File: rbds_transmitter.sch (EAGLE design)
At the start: 50 parts, among them IC1 MAX1551, IC2 TPS61030, IC3 MCP4812, IC4 OPA4743UA, Q1 P-Ch, SW1 FSMSM, U3 ATMEGA328, X1 HD44780LCD-1602, Y1 16Mhz

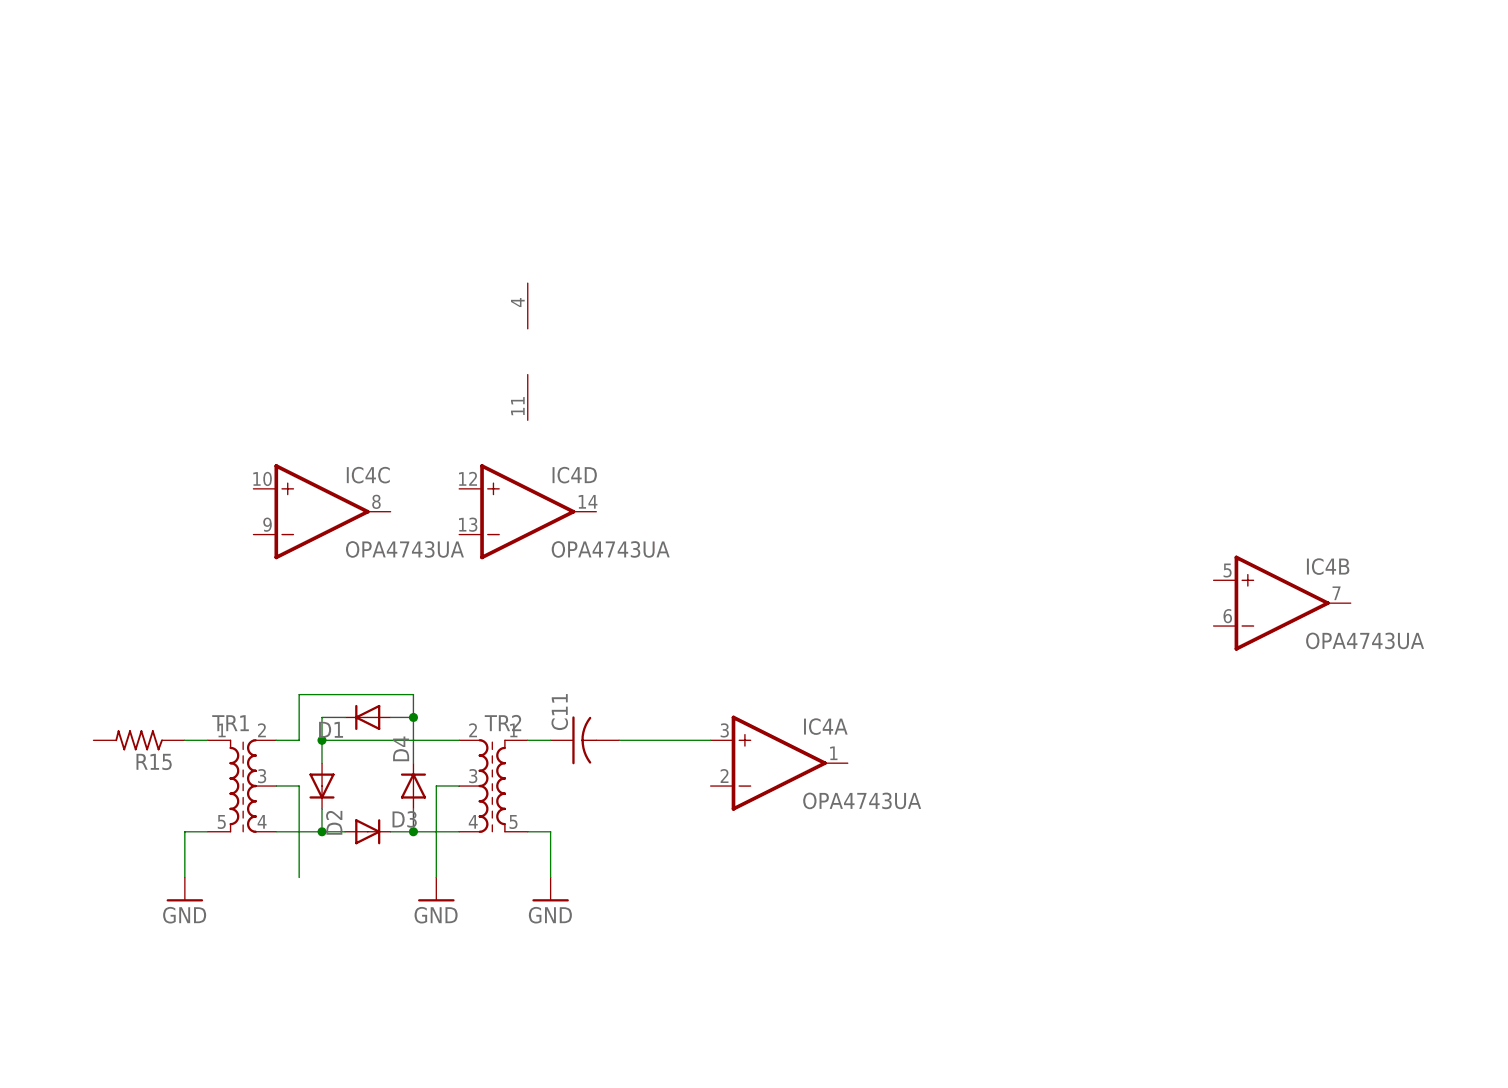
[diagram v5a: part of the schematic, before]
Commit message: adding summing amp
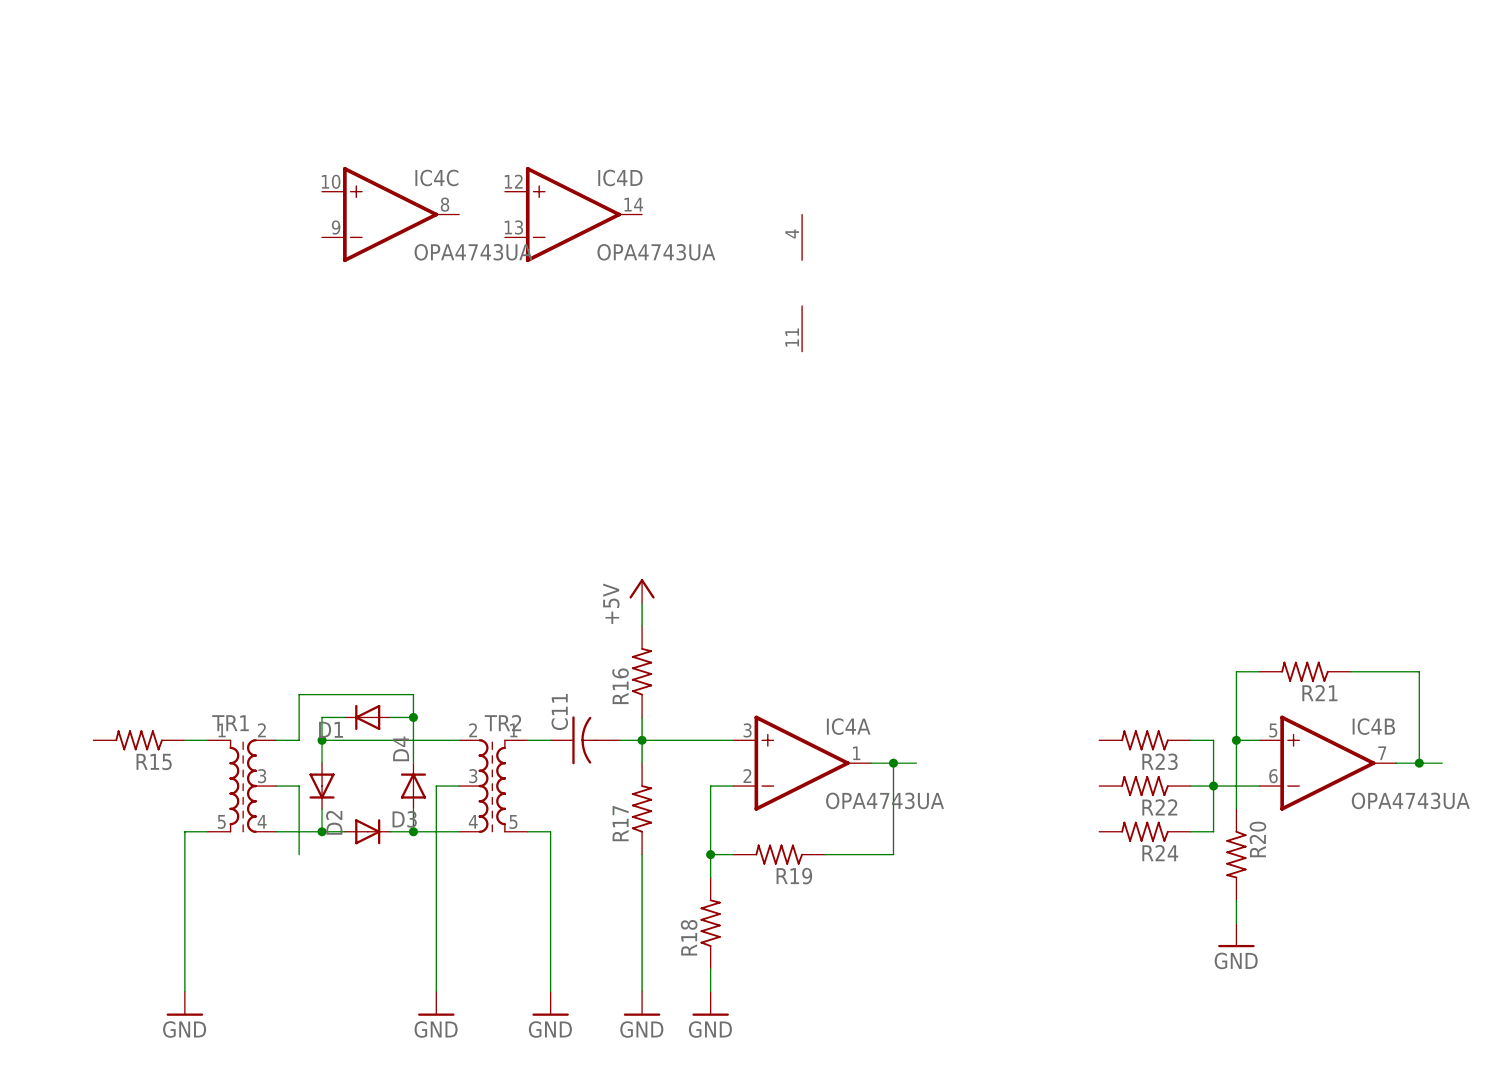
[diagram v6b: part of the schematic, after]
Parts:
- added R16, R17, R18, R19, R20, R21, R22, R23, R24: (no value), adafruit:R-US_R1206
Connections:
- new net N$23: IC4B.+IN, R20.1, R21.2
- new net N$24: IC4A.-IN, R18.2, R19.2
- new net N$25: IC4A.OUT, R19.1
- new net N$26: IC4B.OUT, R21.1
- new net N$27: IC4B.-IN, R22.1, R23.1, R24.1
- net +5V: now also R16.2
- net GND: now also R17.1, R18.1, R20.2
- net N$22: now also R16.1, R17.2
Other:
- moved on the sheet: IC4A, IC4B, IC4C, IC4D
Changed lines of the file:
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@@
 <part name="C11" library="adafruit" deviceset="C-US" device="C1206"/>
 <part name="IC4" library="linear" deviceset="OPA4743" device="UA"/>
+<part name="R16" library="adafruit" deviceset="R-US_" device="R1206"/>
+<part name="R17" library="adafruit" deviceset="R-US_" device="R1206"/>
+<part name="GND26" library="sparkfun" deviceset="GND" device=""/>
+<part name="P+9" library="supply1" deviceset="+5V" device=""/>
+<part name="R18" library="adafruit" deviceset="R-US_" device="R1206"/>
+<part name="R19" library="adafruit" deviceset="R-US_" device="R1206"/>
+<part name="GND27" library="sparkfun" deviceset="GND" device=""/>
+<part name="R20" library="adafruit" deviceset="R-US_" device="R1206"/>
+<part name="R21" library="adafruit" deviceset="R-US_" device="R1206"/>
+<part name="R22" library="adafruit" deviceset="R-US_" device="R1206"/>
+<part name="GND28" library="sparkfun" deviceset="GND" device=""/>
+<part name="R23" library="adafruit" deviceset="R-US_" device="R1206"/>
+<part name="R24" library="adafruit" deviceset="R-US_" device="R1206"/>
 </parts>
 <sheets>
@@
 <instance part="TR1" gate="G$1" x="254" y="-15.24"/>
 <instance part="TR2" gate="G$1" x="279.4" y="-15.24" rot="MR0"/>
-<instance part="GND23" gate="1" x="246.38" y="-27.94"/>
-<instance part="GND24" gate="1" x="274.32" y="-27.94"/>
-<instance part="GND25" gate="1" x="287.02" y="-27.94"/>
+<instance part="GND23" gate="1" x="246.38" y="-40.64"/>
+<instance part="GND24" gate="1" x="274.32" y="-40.64"/>
+<instance part="GND25" gate="1" x="287.02" y="-40.64"/>
 <instance part="R15" gate="G$1" x="241.3" y="-10.16" rot="R180"/>
 <instance part="C11" gate="G$1" x="289.56" y="-10.16" rot="R90"/>
-<instance part="IC4" gate="A" x="312.42" y="-12.7"/>
-<instance part="IC4" gate="B" x="368.3" y="5.08"/>
-<instance part="IC4" gate="C" x="261.62" y="15.24"/>
-<instance part="IC4" gate="D" x="284.48" y="15.24"/>
-<instance part="IC4" gate="P" x="284.48" y="33.02"/>
+<instance part="IC4" gate="A" x="314.96" y="-12.7"/>
+<instance part="IC4" gate="B" x="373.38" y="-12.7"/>
+<instance part="IC4" gate="C" x="269.24" y="48.26"/>
+<instance part="IC4" gate="D" x="289.56" y="48.26"/>
+<instance part="IC4" gate="P" x="314.96" y="40.64"/>
+<instance part="R16" gate="G$1" x="297.18" y="-2.54" rot="R90"/>
+<instance part="R17" gate="G$1" x="297.18" y="-17.78" rot="R90"/>
+<instance part="GND26" gate="1" x="297.18" y="-40.64"/>
+<instance part="P+9" gate="1" x="297.18" y="7.62"/>
+<instance part="R18" gate="G$1" x="304.8" y="-30.48" rot="R90"/>
+<instance part="R19" gate="G$1" x="312.42" y="-22.86" rot="R180"/>
+<instance part="GND27" gate="1" x="304.8" y="-40.64"/>
+<instance part="R20" gate="G$1" x="363.22" y="-22.86" rot="R270"/>
+<instance part="R21" gate="G$1" x="370.84" y="-2.54" rot="R180"/>
+<instance part="R22" gate="G$1" x="353.06" y="-15.24" rot="R180"/>
+<instance part="GND28" gate="1" x="363.22" y="-33.02"/>
+<instance part="R23" gate="G$1" x="353.06" y="-10.16" rot="R180"/>
+<instance part="R24" gate="G$1" x="353.06" y="-20.32" rot="R180"/>
 </instances>
 <busses>
@@
 <pinref part="TR1" gate="G$1" pin="5"/>
 <pinref part="GND23" gate="1" pin="GND"/>
-<wire x1="246.38" y1="-25.4" x2="246.38" y2="-20.32" width="0.1524" layer="91"/>
+<wire x1="246.38" y1="-38.1" x2="246.38" y2="-20.32" width="0.1524" layer="91"/>
 <wire x1="246.38" y1="-20.32" x2="248.92" y2="-20.32" width="0.1524" layer="91"/>
 </segment>
@@
 <pinref part="TR2" gate="G$1" pin="3"/>
 <wire x1="276.86" y1="-15.24" x2="274.32" y2="-15.24" width="0.1524" layer="91"/>
-<wire x1="274.32" y1="-15.24" x2="274.32" y2="-25.4" width="0.1524" layer="91"/>
+<wire x1="274.32" y1="-15.24" x2="274.32" y2="-38.1" width="0.1524" layer="91"/>
 <pinref part="GND24" gate="1" pin="GND"/>
 </segment>
@@
 <pinref part="TR2" gate="G$1" pin="5"/>
 <pinref part="GND25" gate="1" pin="GND"/>
-<wire x1="287.02" y1="-25.4" x2="287.02" y2="-20.32" width="0.1524" layer="91"/>
+<wire x1="287.02" y1="-38.1" x2="287.02" y2="-20.32" width="0.1524" layer="91"/>
 <wire x1="287.02" y1="-20.32" x2="284.48" y2="-20.32" width="0.1524" layer="91"/>
+</segment>
+<segment>
+<pinref part="R17" gate="G$1" pin="1"/>
+<pinref part="GND26" gate="1" pin="GND"/>
+<wire x1="297.18" y1="-38.1" x2="297.18" y2="-22.86" width="0.1524" layer="91"/>
+</segment>
+<segment>
+<pinref part="R18" gate="G$1" pin="1"/>
+<pinref part="GND27" gate="1" pin="GND"/>
+<wire x1="304.8" y1="-38.1" x2="304.8" y2="-35.56" width="0.1524" layer="91"/>
+</segment>
+<segment>
+<pinref part="R20" gate="G$1" pin="2"/>
+<pinref part="GND28" gate="1" pin="GND"/>
+<wire x1="363.22" y1="-30.48" x2="363.22" y2="-27.94" width="0.1524" layer="91"/>
 </segment>
 </net>
@@
 <wire x1="157.48" y1="-2.54" x2="157.48" y2="-5.08" width="0.1524" layer="91"/>
 </segment>
+<segment>
+<pinref part="R16" gate="G$1" pin="2"/>
+<pinref part="P+9" gate="1" pin="+5V"/>
+<wire x1="297.18" y1="5.08" x2="297.18" y2="2.54" width="0.1524" layer="91"/>
+</segment>
 </net>
 <net name="ISP-MISO" class="0">
@@
 <pinref part="TR1" gate="G$1" pin="3"/>
 <wire x1="256.54" y1="-15.24" x2="259.08" y2="-15.24" width="0.1524" layer="91"/>
-<wire x1="259.08" y1="-15.24" x2="259.08" y2="-25.4" width="0.1524" layer="91"/>
+<wire x1="259.08" y1="-15.24" x2="259.08" y2="-22.86" width="0.1524" layer="91"/>
 </segment>
 </net>
@@
 <segment>
 <pinref part="C11" gate="G$1" pin="2"/>
-<wire x1="294.64" y1="-10.16" x2="304.8" y2="-10.16" width="0.1524" layer="91"/>
 <pinref part="IC4" gate="A" pin="+IN"/>
-</segment>
-</net>
+<wire x1="294.64" y1="-10.16" x2="297.18" y2="-10.16" width="0.1524" layer="91"/>
+<pinref part="R16" gate="G$1" pin="1"/>
+<pinref part="R17" gate="G$1" pin="2"/>
+<wire x1="297.18" y1="-10.16" x2="307.34" y2="-10.16" width="0.1524" layer="91"/>
+<wire x1="297.18" y1="-7.62" x2="297.18" y2="-10.16" width="0.1524" layer="91"/>
+<junction x="297.18" y="-10.16"/>
+<wire x1="297.18" y1="-10.16" x2="297.18" y2="-12.7" width="0.1524" layer="91"/>
+</segment>
+</net>
+<net name="N$24" class="0">
+<segment>
+<pinref part="R18" gate="G$1" pin="2"/>
+<wire x1="304.8" y1="-25.4" x2="304.8" y2="-22.86" width="0.1524" layer="91"/>
+<pinref part="IC4" gate="A" pin="-IN"/>
+<wire x1="304.8" y1="-22.86" x2="304.8" y2="-15.24" width="0.1524" layer="91"/>
+<wire x1="304.8" y1="-15.24" x2="307.34" y2="-15.24" width="0.1524" layer="91"/>
+<pinref part="R19" gate="G$1" pin="2"/>
+<wire x1="307.34" y1="-22.86" x2="304.8" y2="-22.86" width="0.1524" layer="91"/>
+<junction x="304.8" y="-22.86"/>
+</segment>
+</net>
+<net name="N$25" class="0">
+<segment>
+<pinref part="R19" gate="G$1" pin="1"/>
+<wire x1="317.5" y1="-22.86" x2="325.12" y2="-22.86" width="0.1524" layer="91"/>
+<wire x1="325.12" y1="-22.86" x2="325.12" y2="-12.7" width="0.1524" layer="91"/>
+<pinref part="IC4" gate="A" pin="OUT"/>
+<wire x1="325.12" y1="-12.7" x2="322.58" y2="-12.7" width="0.1524" layer="91"/>
+<wire x1="325.12" y1="-12.7" x2="327.66" y2="-12.7" width="0.1524" layer="91"/>
+<junction x="325.12" y="-12.7"/>
+</segment>
+</net>
+<net name="N$23" class="0">
+<segment>
+<pinref part="IC4" gate="B" pin="+IN"/>
+<pinref part="R20" gate="G$1" pin="1"/>
+<wire x1="363.22" y1="-17.78" x2="363.22" y2="-10.16" width="0.1524" layer="91"/>
+<wire x1="363.22" y1="-10.16" x2="365.76" y2="-10.16" width="0.1524" layer="91"/>
+<junction x="363.22" y="-10.16"/>
+<wire x1="363.22" y1="-10.16" x2="363.22" y2="-2.54" width="0.1524" layer="91"/>
+<pinref part="R21" gate="G$1" pin="2"/>
+<wire x1="363.22" y1="-2.54" x2="365.76" y2="-2.54" width="0.1524" layer="91"/>
+</segment>
+</net>
+<net name="N$26" class="0">
+<segment>
+<pinref part="R21" gate="G$1" pin="1"/>
+<wire x1="375.92" y1="-2.54" x2="383.54" y2="-2.54" width="0.1524" layer="91"/>
+<wire x1="383.54" y1="-2.54" x2="383.54" y2="-12.7" width="0.1524" layer="91"/>
+<pinref part="IC4" gate="B" pin="OUT"/>
+<wire x1="383.54" y1="-12.7" x2="381" y2="-12.7" width="0.1524" layer="91"/>
+<wire x1="383.54" y1="-12.7" x2="386.08" y2="-12.7" width="0.1524" layer="91"/>
+<junction x="383.54" y="-12.7"/>
+</segment>
+</net>
+<net name="N$27" class="0">
+<segment>
+<pinref part="IC4" gate="B" pin="-IN"/>
+<wire x1="365.76" y1="-15.24" x2="360.68" y2="-15.24" width="0.1524" layer="91"/>
+<pinref part="R22" gate="G$1" pin="1"/>
+<junction x="360.68" y="-15.24"/>
+<wire x1="360.68" y1="-15.24" x2="358.14" y2="-15.24" width="0.1524" layer="91"/>
+<pinref part="R24" gate="G$1" pin="1"/>
+<wire x1="358.14" y1="-20.32" x2="360.68" y2="-20.32" width="0.1524" layer="91"/>
+<wire x1="360.68" y1="-20.32" x2="360.68" y2="-15.24" width="0.1524" layer="91"/>
+<pinref part="R23" gate="G$1" pin="1"/>
+<wire x1="358.14" y1="-10.16" x2="360.68" y2="-10.16" width="0.1524" layer="91"/>
+<wire x1="360.68" y1="-10.16" x2="360.68" y2="-15.24" width="0.1524" layer="91"/>
+</segment>
+</net>

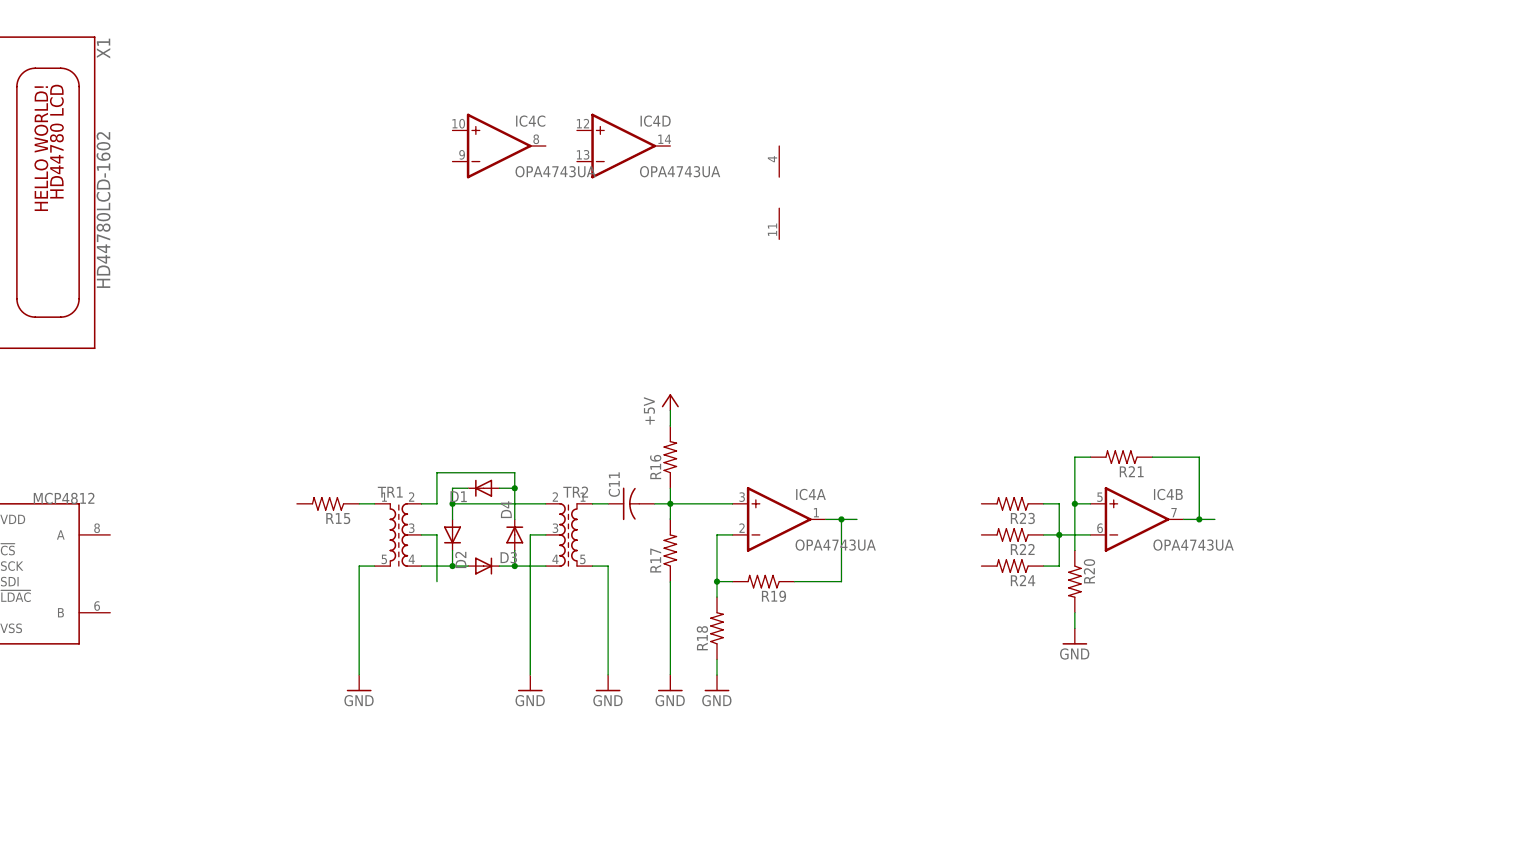
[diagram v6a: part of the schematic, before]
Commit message: added low pass filter
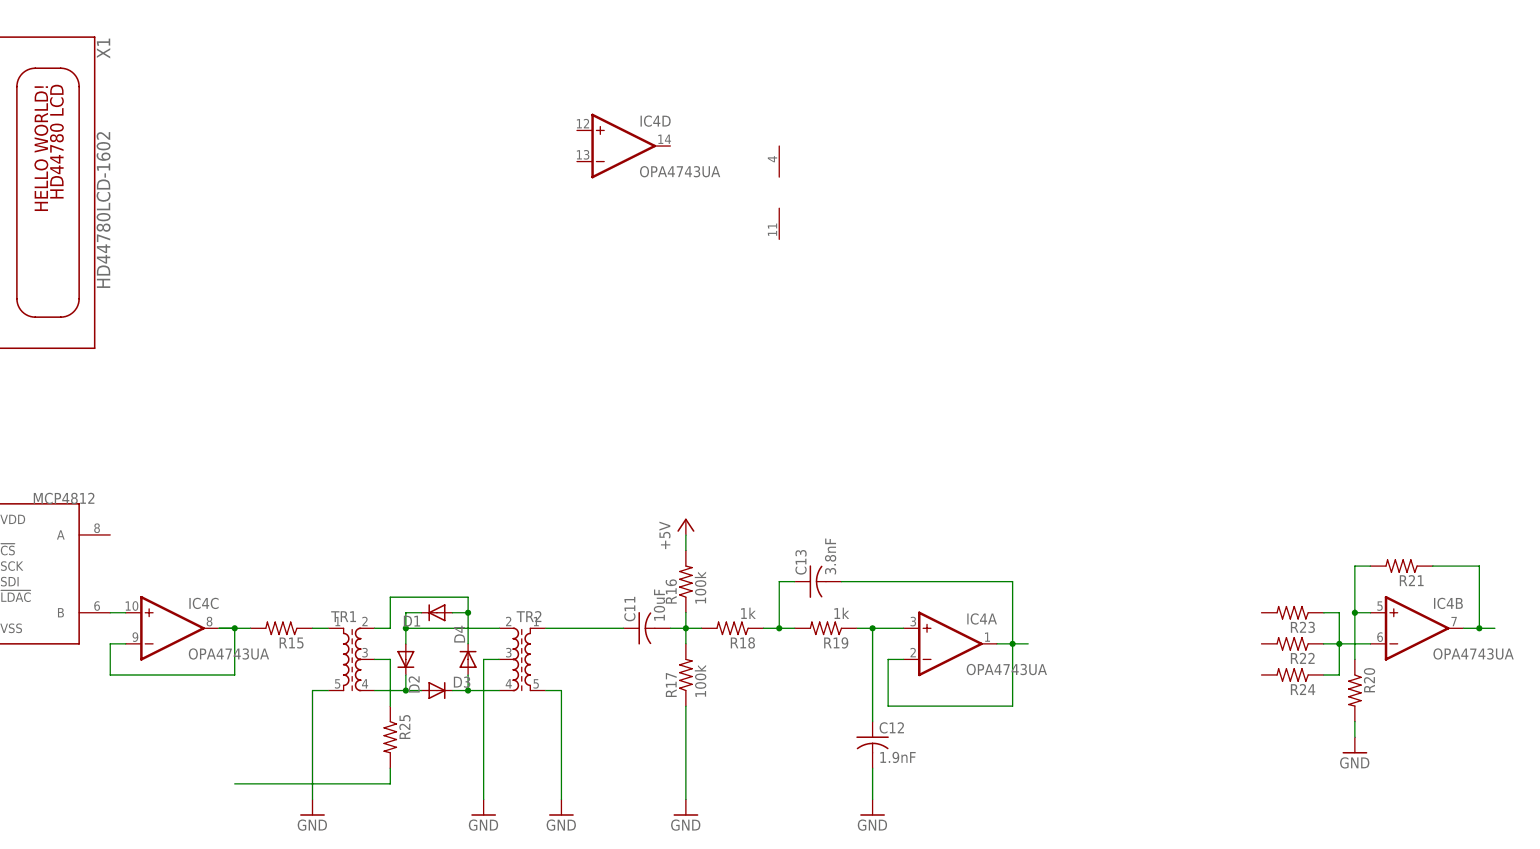
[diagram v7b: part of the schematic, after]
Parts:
- added C12: 1.9nF, adafruit:C-USC1206
- added C13: 3.8nF, adafruit:C-USC1206
- added R25: (no value), adafruit:R-US_R1206
- C11: value (none) -> 10uF
- R16, R17: value (none) -> 100k
- R18, R19: value (none) -> 1k
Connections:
- new net N$28: IC3.B, IC4C.+IN
- new net N$29: IC4C.-IN, IC4C.OUT, R15.2
- new net N$30: R25.2
- new net N$31: C12.1, IC4A.+IN, R19.1
- net GND: now also C12.2; no longer R18.1
- net N$19: now also R25.1
- net N$22: now also R18.2; no longer IC4A.+IN
- net N$24: now also C13.2, IC4A.OUT; no longer R18.2, R19.2
- net N$25: now also C13.1, R18.1, R19.2; no longer IC4A.OUT, R19.1
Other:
- moved on the sheet: C11, D1, D2, D3, D4, IC4A, IC4B, IC4C, R15, R16, R17, R18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
